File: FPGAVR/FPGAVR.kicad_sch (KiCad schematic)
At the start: 26 parts, among them J1 HDMI_A, J3 USB_C_Receptacle, U1 ICE5LP1K-SG48, U2 RP2040, U3 IIM-42652, U4 W25Q128JVS, Y1 Crystal_GND2

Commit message: Worked on the schematic and the HDMI verilog core
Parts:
- removed U3: IIM-42652, Package_LGA:Bosch_LGA-14_3x2.5mm_P0.5mm, symbol Sensor_Motion:IIM-42652
- added C18: 0.1μf, symbol Device:C
- added C19: 2.2μf, symbol Device:C
- added C20, C21: 10nf, symbol Device:C
- added R3, R4: 27Ω, symbol Device:R
- added U3: NCP1117-1.5_SOT223, Package_TO_SOT_SMD:SOT-223-3_TabPin2, symbol Regulator_Linear:NCP1117-1.5_SOT223
- added U5: IIM-42652, Package_LGA:Bosch_LGA-14_3x2.5mm_P0.5mm, symbol Sensor_Motion:IIM-42652
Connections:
- net +1V1: now also C16.1, U1.33 (VCCIO_0)
- net +3V3: now also J1.17 (GND), J1.SH, J3.A1 (GND), J3.A12 (GND), J3.B1 (GND), J3.B12 (GND), J3.SH (SHIELD), C18.1, C18.2, C19.1, C19.2, C20.2, C21.1, C21.2, U3.1 (GND), U3.2 (VO), U5.6 (GND), U5.7 (GND), U5.8 (VDD); no longer C16.1, U1.33 (VCCIO_0)
- net AP_CS: now also U5.12 (AP_CS)
- net AP_SCL: now also U5.13 (AP_SCL/AP_SCLK)
- net AP_SD0: now also U5.1 (AP_SDO/AP_AD0)
- net AP_SDA: now also U5.14 (AP_SDA/AP_SDIO/AP_SDI)
- net USBD+: now also J3.B6 (D+), R4.1
- net USBD-: now also J3.B7 (D-), R3.1
- net XIN: now also U5.9 (INT2/FSYNC/CLKIN)
- net D2-: now reaches U1.23 (IOT_37a)
- net D2-: now also J1.3 (D2-)
- net D2+: now reaches U1.25 (IOT_36b)
- net D2+: now also J1.1 (D2+)
- net D1-: now reaches U1.26 (IOT_39a)
- net D1-: now also J1.6 (D1-)
- net D1+: now reaches U1.27 (IOT_38b)
- net D1+: now also J1.4 (D1+)
- net D0+: now reaches U1.28 (IOT_41a)
- net D0+: now also J1.7 (D0+)
- net D0-: now reaches U1.31 (IOT_42b)
- net D0-: now also J1.9 (D0-)
- net CK+: now reaches U1.32 (IOT_43a)
- net CK+: now also J1.10 (CK+)
- net CK-: now reaches U1.34 (IOT_44b)
- net CK-: now also J1.12 (CK-)
- net GPIO2: now reaches U1.35 (IOT_46b_G0)
- net GPIO2: now also U2.4 (GPIO2)
- net GPIO1: now reaches U1.36 (IOT_48b)
- net GPIO1: now also U2.3 (GPIO1)
- net GPIO3: now reaches U1.37 (IOT_45a_G1)
- net GPIO3: now also U2.5 (GPIO3)
- net TMDSD0S: now reaches U1.39 (RGB0)
- net TMDSD0S: now also J1.8 (D0S)
- net TMDSD1S: now reaches U1.40 (RGB1)
- net TMDSD1S: now also J1.5 (D1S)
- net TMDSD2S: now reaches U1.41 (RGB2)
- net TMDSD2S: now also J1.2 (D2S)
- net GPIO0: now reaches U1.43 (IOT_49a)
- net GPIO0: now also U2.2 (GPIO0)
- net at C17.2: now also U5.5 (VDDIO)
- net SCL: now reaches J1.15 (SCL)
- net SDA: now reaches J1.16 (SDA)
- net +5V: now reaches J1.18 (+5V)
- net +5V: now also J3.A4 (VBUS), J3.A9 (VBUS), J3.B4 (VBUS), J3.B9 (VBUS), C20.1, U3.3 (VI)
- net at U2.46 (USB_DM): now also R3.2
- net at U2.47 (USB_DP): now also R4.2
- no-connect marks 0 -> 9
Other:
- moved on the sheet: C17, J1, R1, R2

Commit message: Worked on the schematic mostly
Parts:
- added D4, D5: Conn_01x24_Pin, symbol Connector:Conn_01x24_Pin
- added J2: Conn_01x20_Pin, symbol Connector:Conn_01x20_Pin
- added J5: Conn_01x14_Pin, symbol Connector:Conn_01x14_Pin
- added R5: 10k, symbol Device:R
- added R6: 1k, symbol Device:R
- added SW1: SW_Push, symbol Switch:SW_Push
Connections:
- net +1V1: no longer C16.1, U1.33 (VCCIO_0)
- net +3V3: now also C16.1, U1.33 (VCCIO_0), D4.1 (Pin_1), D4.10 (Pin_10), D4.12 (Pin_12), D4.13 (Pin_13), D4.14 (Pin_14), D4.17 (Pin_17), D4.18 (Pin_18), D4.7 (Pin_7), D5.1 (Pin_1), D5.10 (Pin_10), D5.12 (Pin_12), D5.13 (Pin_13), D5.14 (Pin_14), D5.17 (Pin_17), D5.18 (Pin_18), D5.7 (Pin_7), R5.1, SW1.1
- net CK+: no longer U1.32 (IOT_43a)
- net CK-: no longer U1.34 (IOT_44b)
- net D0+: no longer U1.28 (IOT_41a)
- net D0-: no longer U1.31 (IOT_42b)
- net D1+: no longer U1.27 (IOT_38b)
- net D1-: no longer U1.26 (IOT_39a)
- net D2+: no longer U1.25 (IOT_36b)
- net D2-: no longer U1.23 (IOT_37a)
- net GPIO0: now also U1.42 (IOT_51a), J2.1 (Pin_1); no longer U1.43 (IOT_49a)
- net GPIO1: now also U1.38 (IOT_50b), J2.2 (Pin_2); no longer U1.36 (IOT_48b)
- net GPIO2: now also U1.43 (IOT_49a), J2.3 (Pin_3); no longer U1.35 (IOT_46b_G0)
- net GPIO3: now also U1.36 (IOT_48b), J2.4 (Pin_4); no longer U1.37 (IOT_45a_G1)
- net QSPI_SCLK: now also U1.26 (IOT_39a)
- net QSPI_SD0: now also U1.28 (IOT_41a)
- net QSPI_SD1: now also U1.31 (IOT_42b)
- net QSPI_SD2: now also U1.32 (IOT_43a)
- net QSPI_SD3: now also U1.34 (IOT_44b)
- net TMDSD0S: now also U1.25 (IOT_36b); no longer U1.39 (RGB0)
- net TMDSD1S: now also U1.23 (IOT_37a); no longer U1.40 (RGB1)
- net TMDSD2S: now also U1.27 (IOT_38b); no longer U1.41 (RGB2)
- net QSPI_SS: now reaches U4.1 (~{CS})
- net QSPI_SS: now also U1.37 (IOT_45a_G1), U2.56 (~{QSPI_SS}), R5.2, R6.2
- net GPIO8: now reaches U2.11 (GPIO8)
- net GPIO9: now reaches U2.12 (GPIO9)
- net GPI10: now reaches U2.13 (GPIO10)
- net GPI11: now reaches U2.14 (GPIO11)
- net GPI12: now reaches U2.15 (GPIO12)
- net GPI13: now reaches U2.16 (GPIO13)
- net GPI14: now reaches U2.17 (GPIO14)
- net GPI15: now reaches U2.18 (GPIO15)
- net GPI16: now reaches U2.27 (GPIO16)
- net GPI17: now reaches U2.28 (GPIO17)
- net GPI18: now reaches U2.29 (GPIO18)
- net GPI19: now reaches U2.30 (GPIO19)
- net GPI20: now reaches U2.31 (GPIO20)
- net GPI20: now also J5.1 (Pin_1)
- net GPI21: now reaches U2.32 (GPIO21)
- net GPI21: now also J5.2 (Pin_2)
- net GPI22: now reaches U2.34 (GPIO22)
- net GPI22: now also J5.3 (Pin_3)
- net GPI23: now reaches U2.35 (GPIO23)
- net GPI23: now also J5.4 (Pin_4)
- net GPI24: now reaches U2.36 (GPIO24)
- net GPI24: now also J5.5 (Pin_5)
- net GPI25: now reaches U2.37 (GPIO25)
- net GPI25: now also J5.6 (Pin_6)
- net GPI26: now reaches U2.38 (GPIO26/ADC0)
- net GPI26: now also J5.7 (Pin_7)
- net GPI27: now reaches U2.39 (GPIO27/ADC1)
- net GPI27: now also J5.8 (Pin_8)
- net GPI28: now reaches U2.40 (GPIO28/ADC2)
- net GPI28: now also J5.9 (Pin_9)
- net GPI29: now reaches U2.41 (GPIO29/ADC3)
- net GPI29: now also J5.10 (Pin_10)
- net GPIO4: now reaches U2.6 (GPIO4)
- net GPIO4: now also J2.5 (Pin_5)
- net GPIO5: now reaches U2.7 (GPIO5)
- net GPIO6: now reaches U2.8 (GPIO6)
- net GPIO7: now reaches U2.9 (GPIO7)
- new net: R6.1, SW1.2
- new net DSI_CLKN: D4.9 (Pin_9)
- new net DSI_CLKN1: D5.9 (Pin_9)
- new net DSI_CLKP: D4.11 (Pin_11)
- new net DSI_CLKP1: D5.11 (Pin_11)
- new net DSI_D0N: D4.3 (Pin_3)
- new net DSI_D0N1: D5.3 (Pin_3)
- new net DSI_D0P: D4.5 (Pin_5)
- new net DSI_D0P1: D5.5 (Pin_5)
- new net ELVDD: D4.20 (Pin_20), D4.22 (Pin_22), D4.24 (Pin_24)
- new net ELVDD1: D5.20 (Pin_20), D5.22 (Pin_22), D5.24 (Pin_24)
- new net ELVSS: D4.19 (Pin_19), D4.21 (Pin_21), D4.23 (Pin_23)
- new net ELVSS1: D5.19 (Pin_19), D5.21 (Pin_21), D5.23 (Pin_23)
- new net IOT_46b_G0: J5.14 (Pin_14), U1.35 (IOT_46b_G0)
- new net NC(MTP): D4.6 (Pin_6)
- new net NC(MTP)1: D5.6 (Pin_6)
- new net RGB0: J5.13 (Pin_13), U1.39 (RGB0)
- new net RGB1: J5.12 (Pin_12), U1.40 (RGB1)
- new net RGB2: J5.11 (Pin_11), U1.41 (RGB2)
- new net SWIRE: D4.4 (Pin_4)
- new net SWIRE1: D5.4 (Pin_4)
- new net TE: D4.8 (Pin_8)
- new net TE1: D5.8 (Pin_8)
- new net VCI: D4.16 (Pin_16)
- new net VCI1: D5.16 (Pin_16)
- new net VDDIO: D4.15 (Pin_15)
- new net VDDIO1: D5.15 (Pin_15)
- new net XRES: D4.2 (Pin_2)
- new net XRES1: D5.2 (Pin_2)
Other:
- note added: "This is for Display 1"
- note added: "This is for Display 2"
- moved on the sheet: C16, U1A

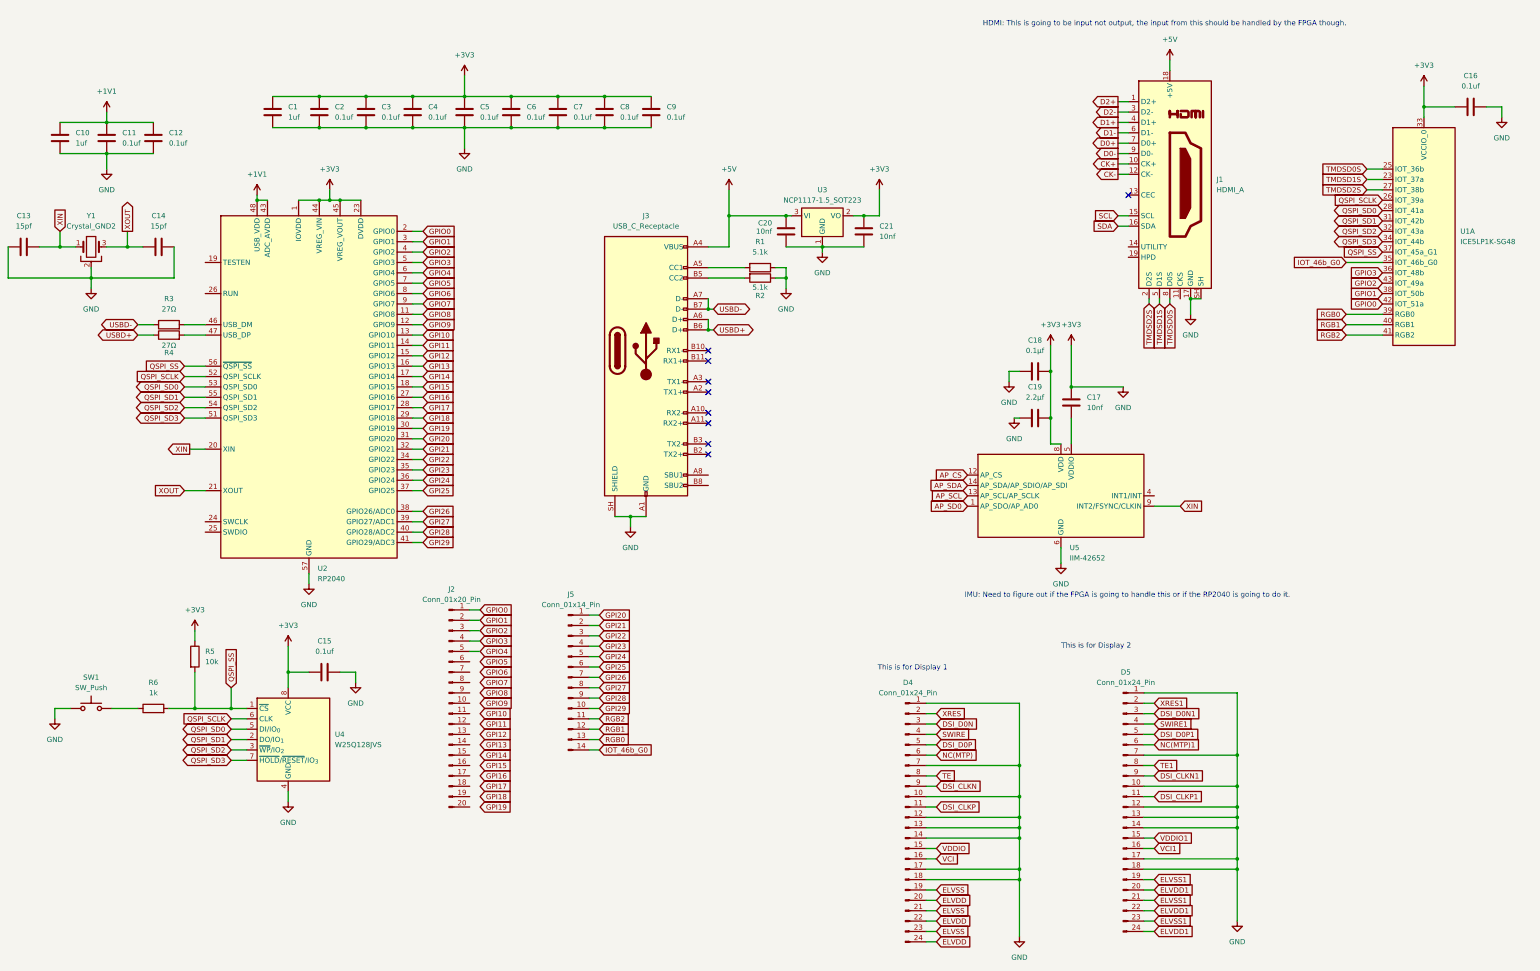
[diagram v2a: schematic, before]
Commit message: Added a MT48LC32M8A2P. I will probably replace it though
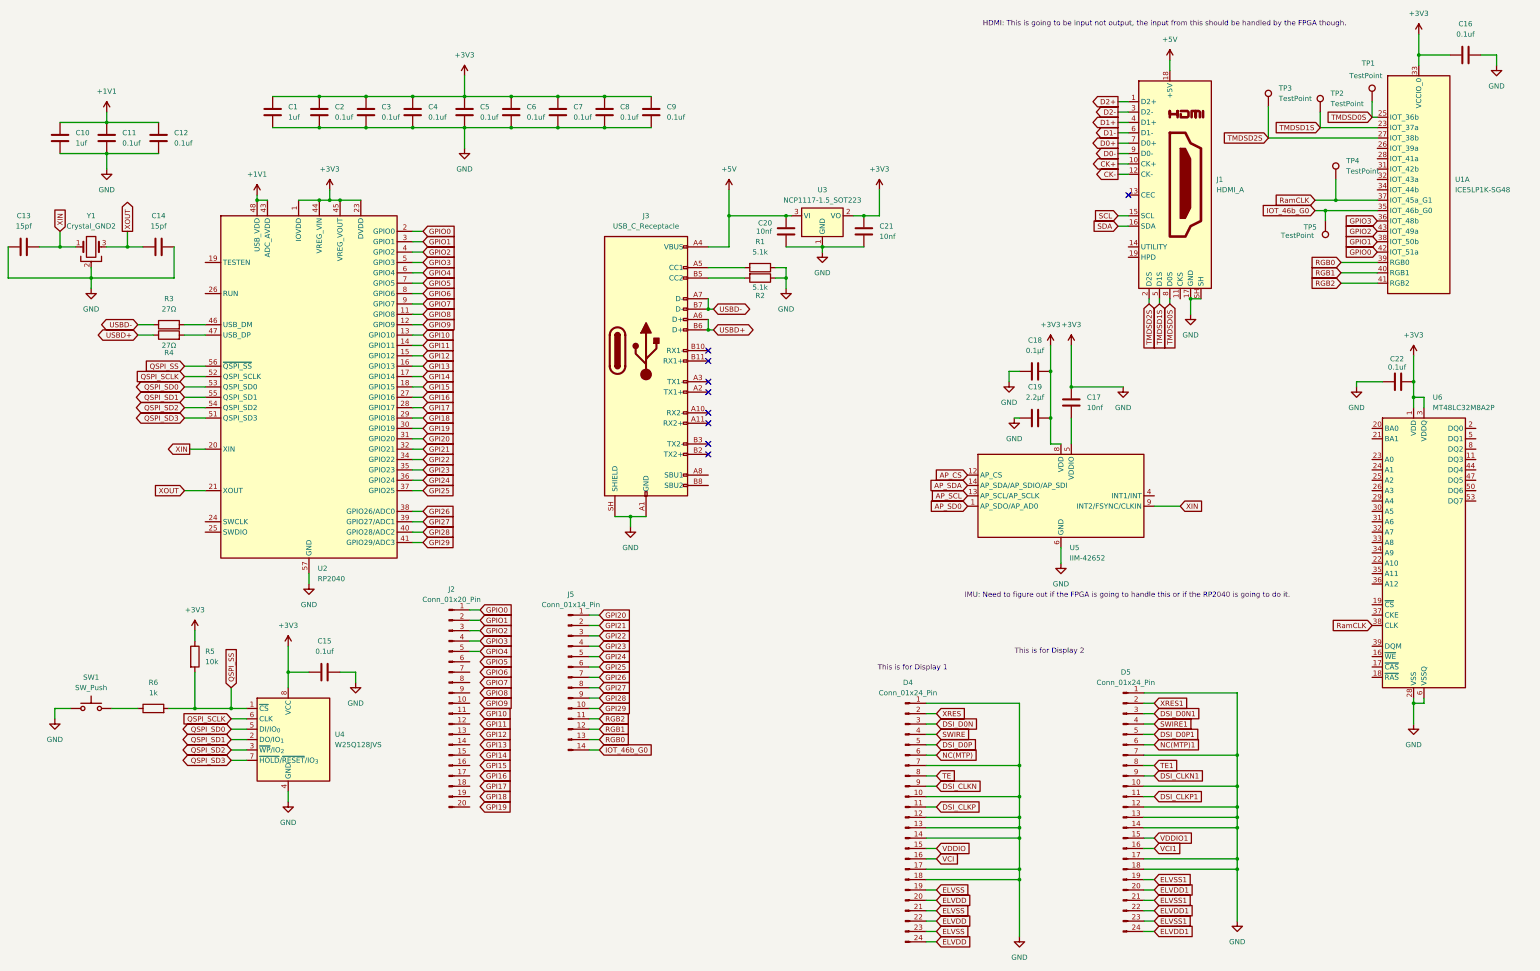
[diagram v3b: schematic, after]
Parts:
- added C22: 0.1uf, symbol Device:C
- added TP1, TP2, TP3, TP4, TP5: TestPoint, symbol Connector:TestPoint
- added U6: MT48LC32M8A2P, Package_SO:TSOP-II-54_22.2x10.16mm_P0.8mm, symbol Memory_RAM:MT48LC32M8A2P
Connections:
- net +3V3: now also C22.1, C22.2, U6.1 (VDD), U6.12 (VSSQ), U6.14 (VDD), U6.27 (VDD), U6.28 (VSS), U6.3 (VDDQ), U6.41 (VSS), U6.43 (VDDQ), U6.46 (VSSQ), U6.49 (VDDQ), U6.52 (VSSQ), U6.54 (VSS), U6.6 (VSSQ), U6.9 (VDDQ)
- net IOT_46b_G0: now also TP5.1
- net QSPI_SCLK: no longer U1.26 (IOT_39a)
- net QSPI_SD0: no longer U1.28 (IOT_41a)
- net QSPI_SD1: no longer U1.31 (IOT_42b)
- net QSPI_SD2: no longer U1.32 (IOT_43a)
- net QSPI_SD3: no longer U1.34 (IOT_44b)
- net QSPI_SS: no longer U1.37 (IOT_45a_G1)
- net TMDSD0S: now also TP1.1
- net TMDSD1S: now also TP2.1
- net TMDSD2S: now also TP3.1
- new net RamCLK: TP4.1, U1.37 (IOT_45a_G1), U6.38 (CLK)
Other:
- moved on the sheet: C12, C16, U1A
